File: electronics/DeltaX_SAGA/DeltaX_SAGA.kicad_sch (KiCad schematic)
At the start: 81 parts, among them J1 USB_B_Micro, J10 Motor3_Encoder, J11 Motor1_OUT, J12 Motor2_OUT, J13 Motor3_OUT, J2 Programmer, J3 SERVO, J5 Power(6-38V), J6 Thrower Signal, J7 Thrower Power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

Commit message: schematic updated
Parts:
- removed D3, D4, D5: 1N53xxB, Diode_SMD:D_0603_1608Metric, symbol Diode:1N53xxB
- removed J11: Motor1_OUT, Connector_PinHeader_2.54mm:PinHeader_1x02_P2.54mm_Vertical_SMD_Pin1Right, symbol Connector_Generic:Conn_01x02
- removed J12: Motor2_OUT, Connector_PinHeader_2.54mm:PinHeader_1x02_P2.54mm_Vertical_SMD_Pin1Right, symbol Connector_Generic:Conn_01x02
- removed J13: Motor3_OUT, Connector_PinHeader_2.54mm:PinHeader_1x02_P2.54mm_Vertical_SMD_Pin1Right, symbol Connector_Generic:Conn_01x02
- removed J5: Power(6-38V), Connector_PinHeader_2.54mm:PinHeader_1x02_P2.54mm_Vertical_SMD_Pin1Right, symbol Connector_Generic:Conn_01x02
- removed J7: Thrower Power, Connector_PinHeader_2.54mm:PinHeader_1x02_P2.54mm_Vertical_SMD_Pin1Right, symbol Connector_Generic:Conn_01x02
- removed Q2, Q3: BUK6Y10, BUK6Y10:TO127P600X120-5N, symbol BUK6Y10:BUK6Y10
- removed R5, R7, R9: 10, Resistor_SMD:R_0603_1608Metric, symbol Device:R
- removed R6, R8: 100, Resistor_SMD:R_0603_1608Metric, symbol Device:R
- added J11: M12, 1pinSMD:1PinSMD, symbol Connector_Generic:Conn_01x01
- added J12: M21, 1pinSMD:1PinSMD, symbol Connector_Generic:Conn_01x01
- added J13: M22, 1pinSMD:1PinSMD, symbol Connector_Generic:Conn_01x01
- added J14: M31, 1pinSMD:1PinSMD, symbol Connector_Generic:Conn_01x01
- added J15: M33, 1pinSMD:1PinSMD, symbol Connector_Generic:Conn_01x01
- added J16: Thrower+, 1pinSMD:1PinSMD, symbol Connector_Generic:Conn_01x01
- added J17: Thrower-, 1pinSMD:1PinSMD, symbol Connector_Generic:Conn_01x01
- added J4: M11, 1pinSMD:1PinSMD, symbol Connector_Generic:Conn_01x01
- added J5: Battery+, 1pinSMD:1PinSMD, symbol Connector_Generic:Conn_01x01
- added J7: Battery-, 1pinSMD:1PinSMD, symbol Connector_Generic:Conn_01x01
- C10, C14, C17, C20, C21, C22, C23, C29, C30, C31, C32, C33, C34, C35, C36, C37, C38: footprint Capacitor_SMD:C_0603_1608Metric -> Capacitor_SMD:C_0805_2012Metric
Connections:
- net +5VD: now also R1.1; no longer R1.2
- net GND2: now also J17.1 (Pin_1), J7.1 (Pin_1)
- net Motor1_OUT1: now also J4.1 (Pin_1)
- net Motor1_OUT2: now also J11.1 (Pin_1)
- net Motor2_OUT1: now also J12.1 (Pin_1)
- net Motor2_OUT2: now also J13.1 (Pin_1)
- net Motor3_OUT1: now also J14.1 (Pin_1)
- net Motor3_OUT2: now also J15.1 (Pin_1)
- net V+: now also J16.1 (Pin_1), J5.1 (Pin_1)
- net at C26.1, U5.6 (BST): now also L1.1
- net at C26.2: now also U5.5 (SW); no longer L1.1
- net FB: now reaches U5.8 (FB)
- net FB: now also R1.2, R2.2
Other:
- moved on the sheet: C25, C26, C27, L1, Q1, R1, R2, R3

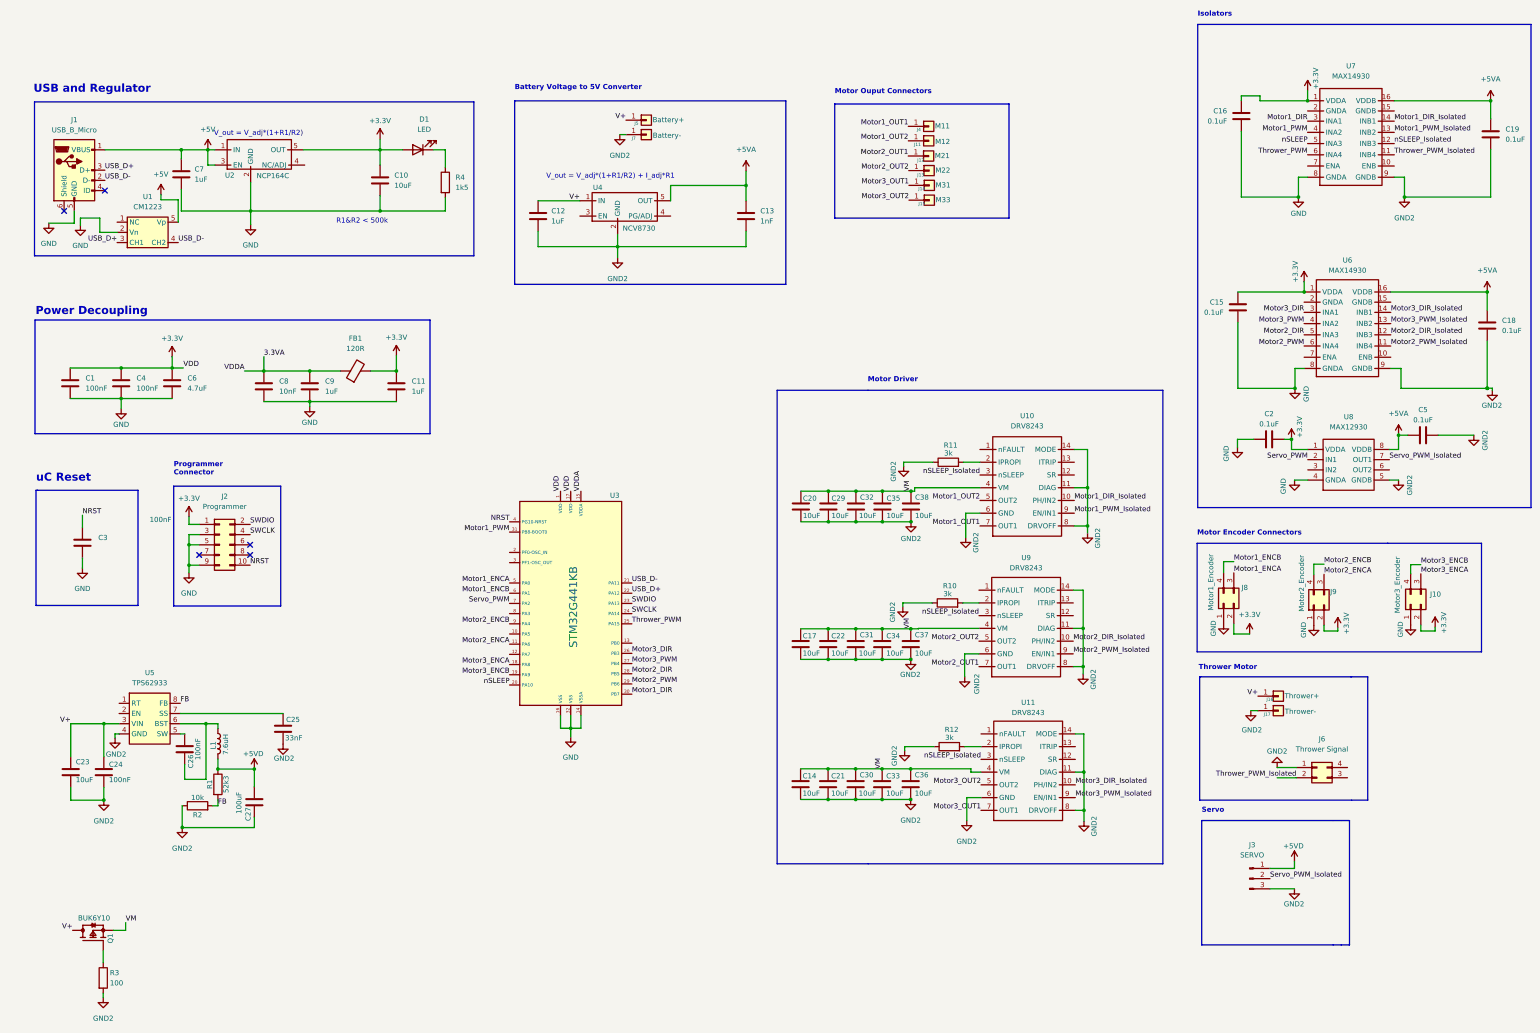
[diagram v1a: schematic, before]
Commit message: schematic board updated
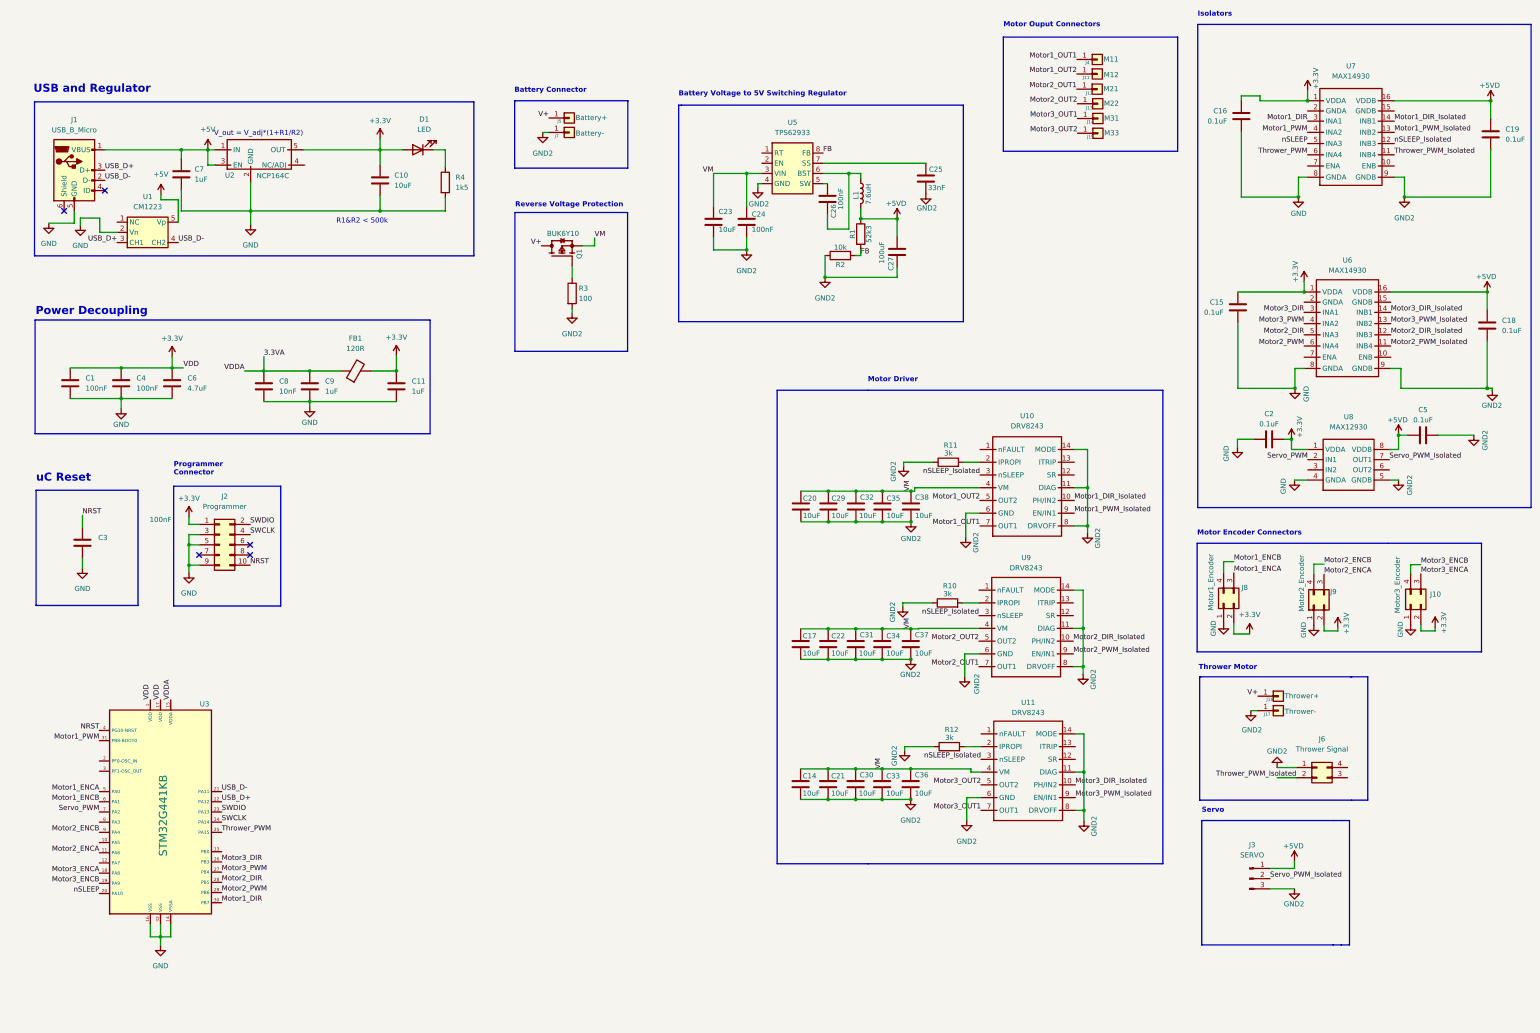
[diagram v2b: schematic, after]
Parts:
- removed C12: 1uF, Capacitor_SMD:C_0603_1608Metric, symbol Device:C
- removed C13: 1nF, Capacitor_SMD:C_0603_1608Metric, symbol Device:C
- removed U4: NCV8730, NCV8730:SOT95P275X110-5N, symbol NCV8730:NCV8730
- C27: footprint Capacitor_SMD:C_0603_1608Metric -> Capacitor_SMD:C_1206_3216Metric
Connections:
- net +5VA is gone; now on net +5VD: C18.2, C19.2, C5.1, U6.16 (VDDB), U7.16 (VDDB), U8.8 (VDDB)
- net V+: no longer C23.1, C24.1, U5.3 (VIN)
- net VM: now also C23.1, C24.1, U5.3 (VIN)
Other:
- note added: "Battery Connector"
- note added: "Battery Voltage to 5V Switching Regulator"
- note added: "Reverse Voltage Protection"
- note removed: "Battery Voltage to 5V Converter"
- note removed: "V_out = V_adj*(1+R1/R2) + I_adj*R1"
- moved on the sheet: C23, C24, C25, C26, C27, J11, J12, J13, J14, J15, J4, J5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

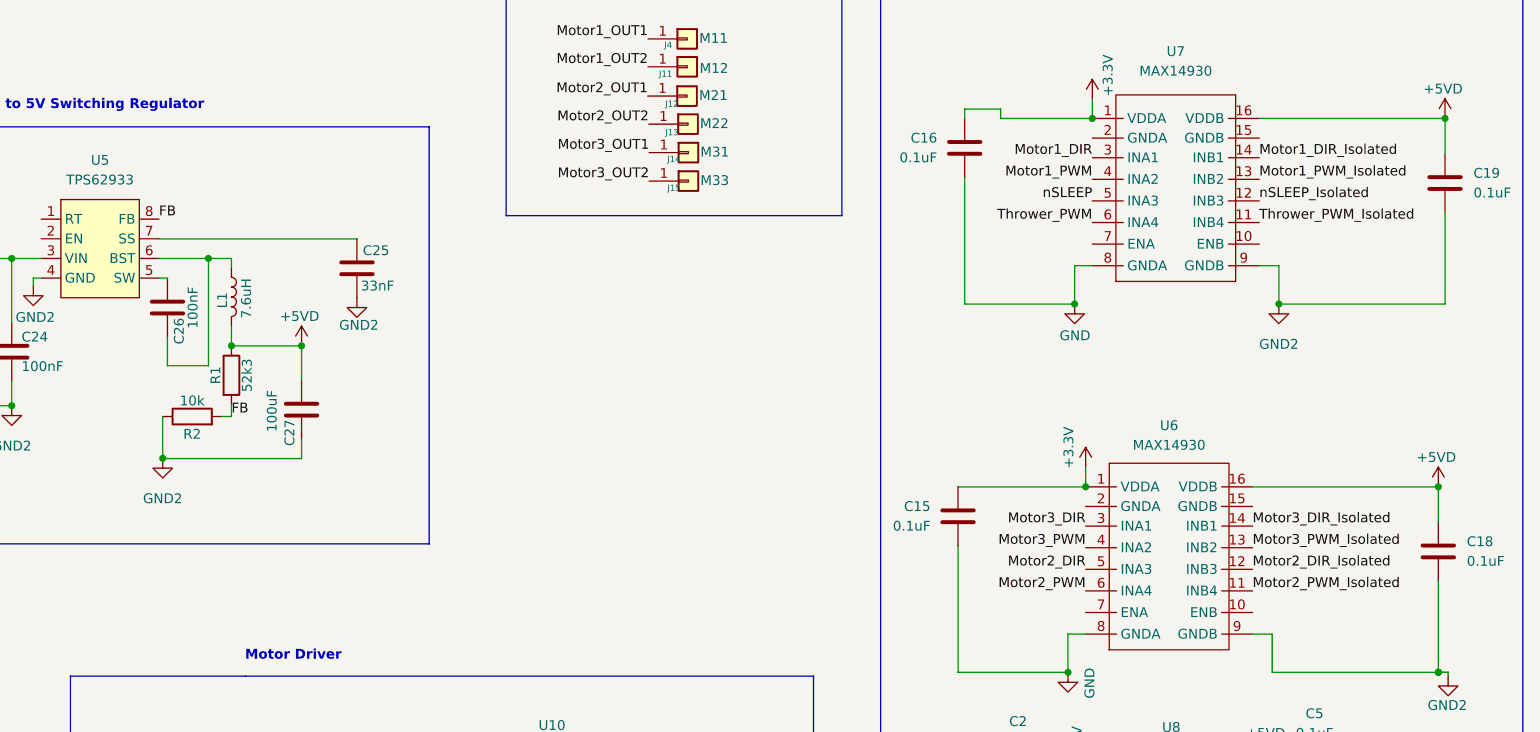
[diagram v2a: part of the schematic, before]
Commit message: schematic board updated
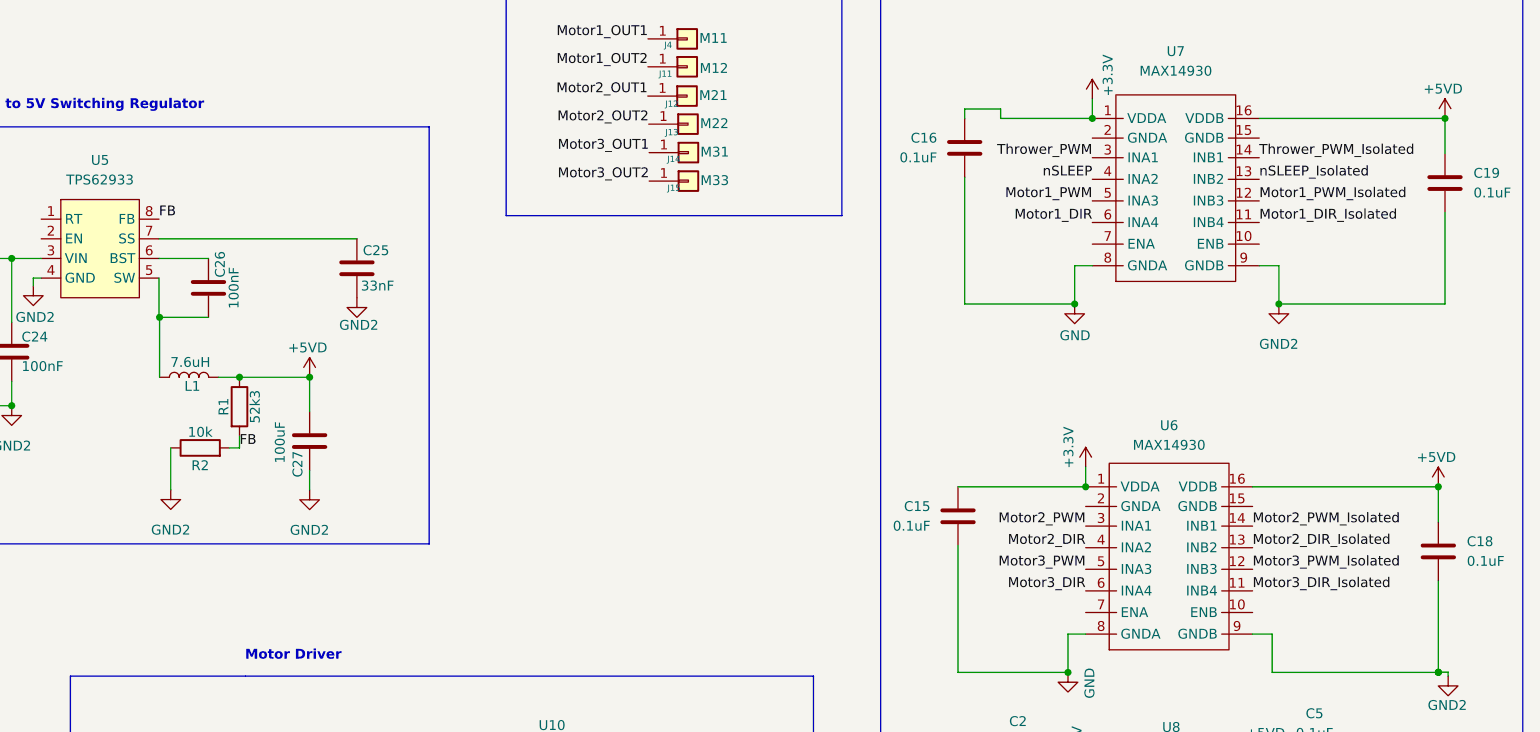
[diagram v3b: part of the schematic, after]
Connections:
- net Motor1_DIR: now also U7.6 (INA4); no longer U7.3 (INA1)
- net Motor1_DIR_Isolated: now also U7.11 (INB4); no longer U7.14 (INB1)
- net Motor1_PWM: now also U7.5 (INA3); no longer U7.4 (INA2)
- net Motor1_PWM_Isolated: now also U7.12 (INB3); no longer U7.13 (INB2)
- net Motor2_DIR: now also U6.4 (INA2); no longer U6.5 (INA3)
- net Motor2_DIR_Isolated: now also U6.13 (INB2); no longer U6.12 (INB3)
- net Motor2_PWM: now also U6.3 (INA1); no longer U6.6 (INA4)
- net Motor2_PWM_Isolated: now also U6.14 (INB1); no longer U6.11 (INB4)
- net Motor3_DIR: now also U6.6 (INA4); no longer U6.3 (INA1)
- net Motor3_DIR_Isolated: now also U6.11 (INB4); no longer U6.14 (INB1)
- net Motor3_PWM: now also U6.5 (INA3); no longer U6.4 (INA2)
- net Motor3_PWM_Isolated: now also U6.12 (INB3); no longer U6.13 (INB2)
- net Thrower_PWM: now also U7.3 (INA1); no longer U7.6 (INA4)
- net Thrower_PWM_Isolated: now also U7.14 (INB1); no longer U7.11 (INB4)
- net nSLEEP: now also U7.4 (INA2); no longer U7.5 (INA3)
- net nSLEEP_Isolated: now also U7.13 (INB2); no longer U7.12 (INB3)
- net at C26.1, U5.6 (BST): no longer L1.1
- net at C26.2, U5.5 (SW): now also L1.1
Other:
- moved on the sheet: C26, C27, L1, R1, R2
